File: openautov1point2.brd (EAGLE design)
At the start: 97 x 77 mm, 78 parts, among them CN1 6p-2.54, CN2 6p-2.54, CN3 6p-2.54, IC1 NC7SZ14M5X, IC2 TJA1049, IC3 NCP1117CORRECT, J3 4p-2.54, Q1 s9013, Q2 s9013, U3 MMA7660FCR1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

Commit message: updated after design review
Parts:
- added CN4: 3p-2.54, Seeed-Connector:H3-2.54
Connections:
- new net VRELAY: CN4.2, D2.C, D3.C, RELAY1.2, RELAY2.2
- net +5V: no longer D2.C, D3.C, RELAY1.2, RELAY2.2
- net 3.3V: now also CN4.3
- net 5V: now also CN4.1
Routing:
- net GND: track 569.7 -> 0.00 mm, vias 33 -> 0
- net 3.3V: track 342.0 -> 0.00 mm, vias 2 -> 0
- net N$10: track 173.8 -> 0.00 mm
- net +5V: track 130.3 -> 0.00 mm
- net 5V: track 107.9 -> 0.00 mm, vias 2 -> 0
- net GPS_RX: track 87.4 -> 0.00 mm, vias 1 -> 0
- net GPS_TX: track 82.3 -> 0.00 mm, vias 2 -> 0
- net SCL: track 78.7 -> 0.00 mm, vias 2 -> 0
- net VBAT: track 72.7 -> 0.00 mm, vias 1 -> 0
- net RFIDTX: track 70.1 -> 0.00 mm, vias 1 -> 0
- net RELAY2: track 66.5 -> 0.00 mm
- net +12V: track 65.9 -> 0.00 mm
- net RTC_INT: track 64.7 -> 0.00 mm, vias 2 -> 0
- net GPS_RESET: track 64.6 -> 0.00 mm, vias 1 -> 0
- net GPS_1PPS: track 62.6 -> 0.00 mm, vias 2 -> 0
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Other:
- board text added: "5V"
- board text added: "VRelay"

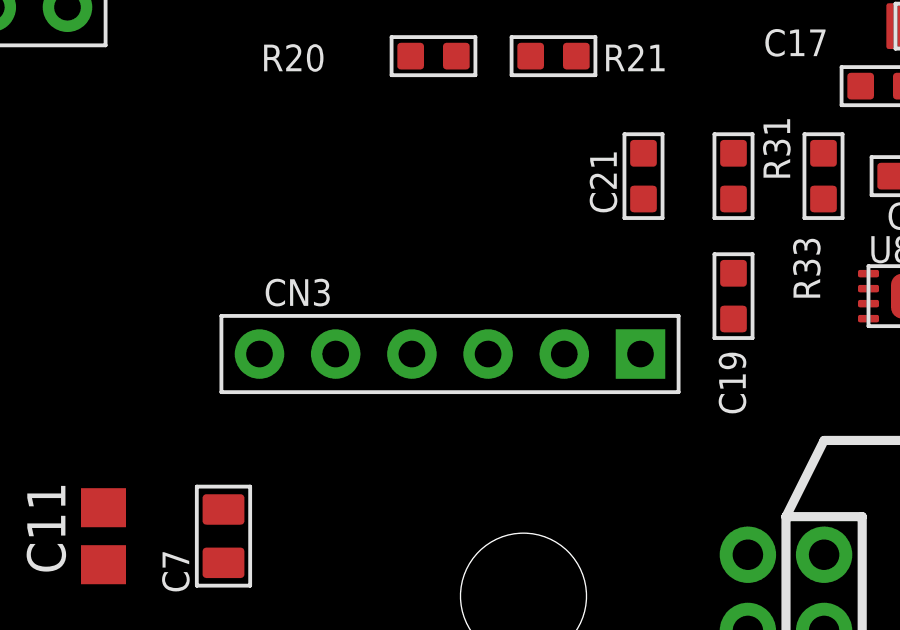
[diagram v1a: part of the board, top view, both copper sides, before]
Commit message: RDM6300 footprint corrected
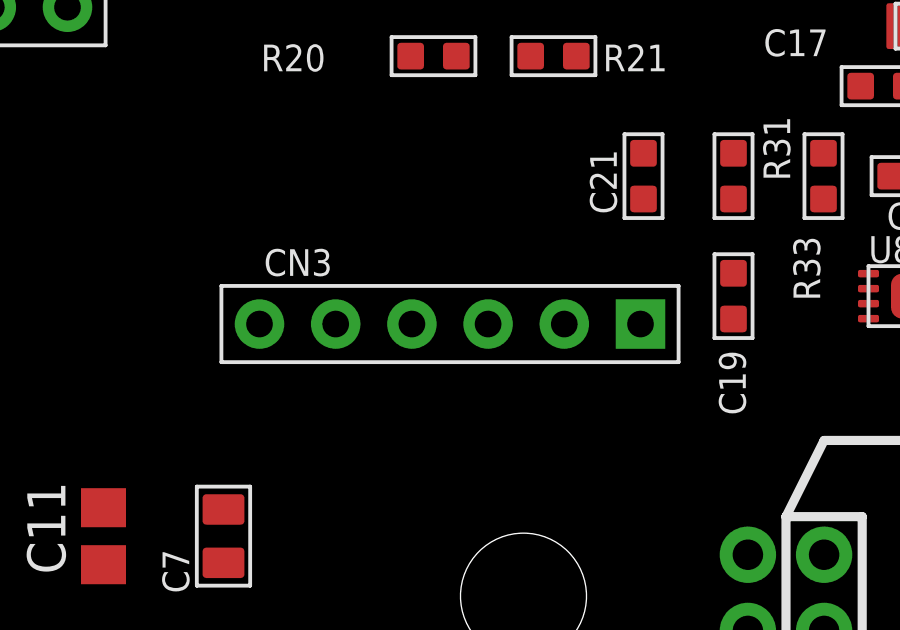
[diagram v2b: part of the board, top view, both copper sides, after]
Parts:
- moved CN3 1.00 mm to (29.6, 55.1)

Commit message: Final update before Production, BOM still needs tidying
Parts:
- removed C2: 100nf, Seeed-Capacitor:C0603
- removed R16: 1K, Seeed-Resistor:R0603
- added C5: 100nf, Seeed-Capacitor:C0603
- added CN5: 3p-2.54, Seeed-Connector:H3-2.54
- added R3: 10K, Seeed-Resistor:R0603
- R2: value 10K -> 1K
- R21: value 3.9K -> 4.7K
- R24, R25: value 3.9K -> 2.2K
- R31, R33: value 10K -> 4.7K
- moved R2 66.3 mm to (88.0, 6.00), turned to 270 degrees
- moved C1 44.0 mm to (53.0, 19.0), turned to 270 degrees
- moved CN4 0.63 mm to (78.0, 51.0)
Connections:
- new net N$2: CN5.2, U5.12
- net 3.3V: now also C1.2; no longer C2.1
- net 5V: now also C5.1; no longer C1.2
- net GND: now also C5.2, CN5.1, R24.1, R3.2; no longer C2.2, R2.1
- net GPS_1PPS: now also R2.1; no longer R16.1
- net N$21: no longer R24.1
- net N$9: now also R2.2; no longer R16.2
- net VBAT: now also R3.1; no longer R2.2
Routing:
- net GND: track 0.00 -> 532.3 mm, vias 0 -> 15
- net 3.3V: track 0.00 -> 382.5 mm, vias 0 -> 5
- net 5V: track 0.00 -> 172.3 mm, vias 0 -> 2
- net N$10: track 0.00 -> 144.5 mm, vias 0 -> 2
- net GPS_TX: track 0.00 -> 82.9 mm, vias 0 -> 1
- net RFIDTX: track 0.00 -> 81.8 mm
- net GPS_RX: track 0.00 -> 80.7 mm, vias 0 -> 1
- net VBAT: track 0.00 -> 71.7 mm, vias 0 -> 3
- net SCL: track 0.00 -> 68.6 mm, vias 0 -> 3
- net STATUSLED: track 0.00 -> 65.8 mm
- net GPS_1PPS: track 0.00 -> 62.2 mm, vias 0 -> 2
- net RTC_INT: track 0.00 -> 62.1 mm
- net RELAY2: track 0.00 -> 60.9 mm, vias 0 -> 1
- net SDA: track 0.00 -> 60.0 mm, vias 0 -> 4
- net BUTTON1: track 0.00 -> 54.3 mm, vias 0 -> 1
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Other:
- board text added: "Ant"
- board text added: "Ext"
- board text added: "Int."
